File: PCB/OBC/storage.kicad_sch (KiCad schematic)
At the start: 2 parts, among them U1 W25Q128JVSIQ

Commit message: Watchdog
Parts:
- removed C3: C, symbol Device:C
- removed U1: W25Q128JVSIQ, SOIC_128JVSIQ_WIN, symbol W25Q128JVSIQ:W25Q128JVSIQ
- added C13: 100nF, symbol Device:C
- added U7: MAX6369KA+T, 21-0078H_MXM, symbol MAX6369KA+T:MAX6369KA+T
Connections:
- net +3V3: now also C13.1, U7.8 (VCC)
- net GND: now also C13.2, U7.2 (GND)
- new net SWD_NRST: U7.7 (*WDO)
- new net rst_wdi: U7.1 (WDI)
- new net set_0: U7.4 (SET0)
- new net set_1: U7.5 (SET1)
- new net set_2: U7.6 (SET2)

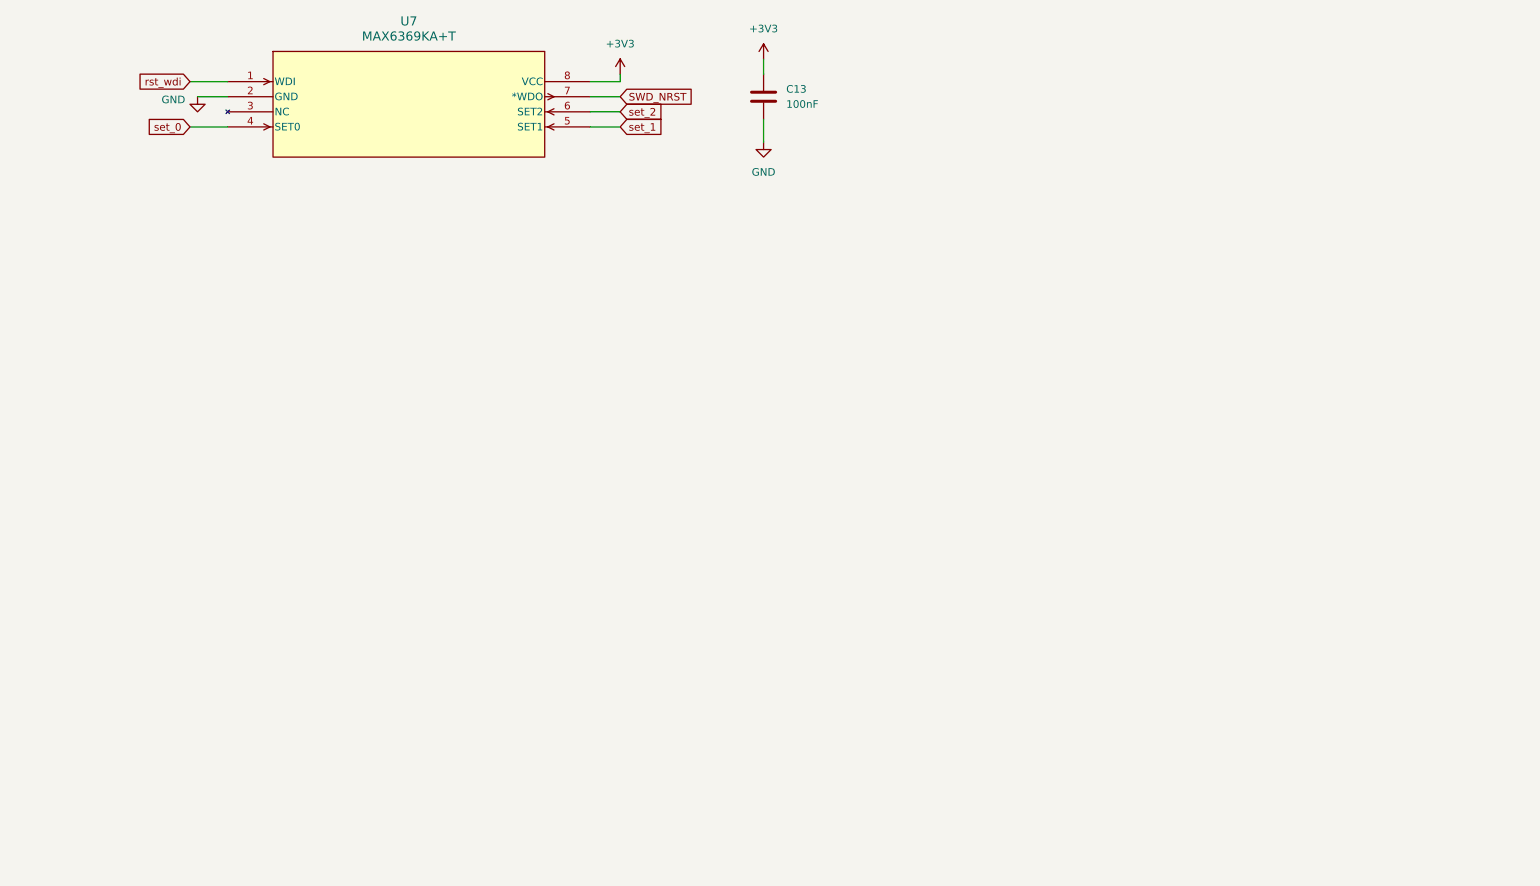
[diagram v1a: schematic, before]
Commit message: Colocacion de OCP, LDO
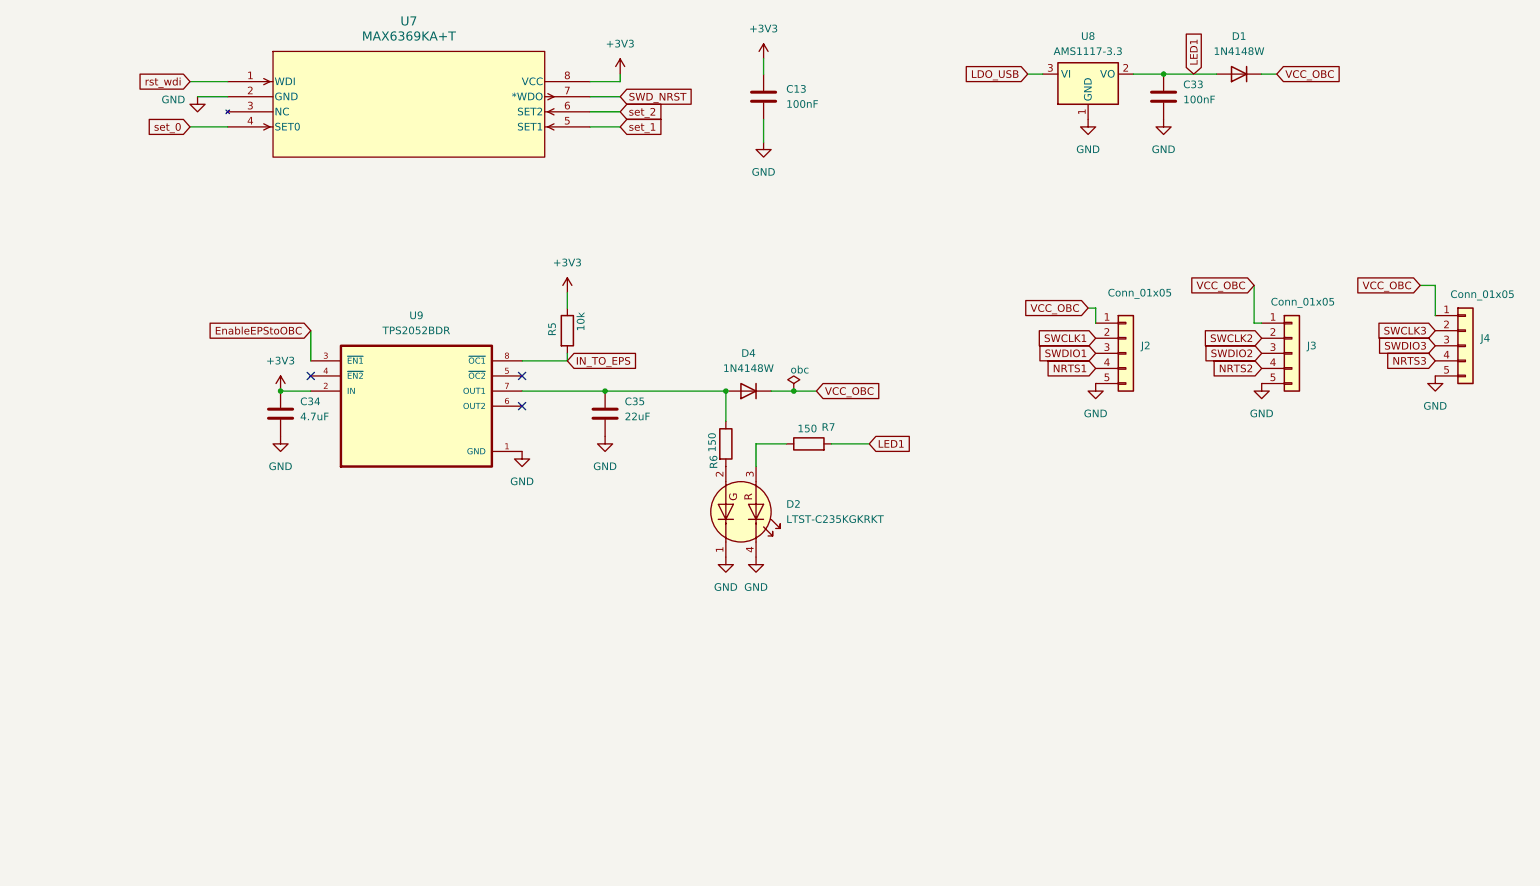
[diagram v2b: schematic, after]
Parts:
- added C33: 100nF, Capacitor_SMD:C_0805_2012Metric_Pad1.18x1.45mm_HandSolder, symbol Device:C
- added C34: 4.7uF, Capacitor_SMD:C_0805_2012Metric_Pad1.18x1.45mm_HandSolder, symbol Device:C
- added C35: 22uF, Capacitor_SMD:C_0805_2012Metric_Pad1.18x1.45mm_HandSolder, symbol Device:C
- added D1, D4: 1N4148W, Diode_SMD:D_SOD-123, symbol Diode:1N4148W
- added D2: LTST-C235KGKRKT, LED_SMD:LED_LiteOn_LTST-C235KGKRKT, symbol LED:LTST-C235KGKRKT
- added J2, J3, J4: Conn_01x05, Connector_PinHeader_2.54mm:PinHeader_1x05_P2.54mm_Vertical_SMD_Pin1Left, symbol Connector_Generic:Conn_01x05
- added R5: 10k, symbol Device:R
- added R6, R7: 150, symbol Device:R
- added U8: AMS1117-3.3, Package_TO_SOT_SMD:SOT-223-3_TabPin2, symbol Regulator_Linear:AMS1117-3.3
- added U9: TPS2052BDR, TPS2052BDR:SOIC127P599X175-8N, symbol TPS2052BDR:TPS2052BDR
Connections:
- net +3V3: now also C34.1, R5.1, U9.2 (IN)
- net GND: now also C33.2, C34.2, C35.2, D2.1 (K2), D2.4 (K1), J2.5 (Pin_5), J3.5 (Pin_5), J4.5 (Pin_5), U8.1 (GND), U9.1 (GND)
- new net: C35.1, D4.2 (A), R6.1, U9.7 (OUT1)
- new net: D2.3 (A1), R7.1
- new net: D2.2 (A2), R6.2
- new net EnableEPStoOBC: U9.3 (~{EN1})
- new net IN_TO_EPS: R5.2, U9.8 (~{OC1})
- new net LDO_USB: U8.3 (VI)
- new net LED1: C33.1, D1.2 (A), R7.2, U8.2 (VO)
- new net NRTS1: J2.4 (Pin_4)
- new net NRTS2: J3.4 (Pin_4)
- new net NRTS3: J4.4 (Pin_4)
- new net SWCLK1: J2.2 (Pin_2)
- new net SWCLK2: J3.2 (Pin_2)
- new net SWCLK3: J4.2 (Pin_2)
- new net SWDIO1: J2.3 (Pin_3)
- new net SWDIO2: J3.3 (Pin_3)
- new net SWDIO3: J4.3 (Pin_3)
- new net VCC_OBC: D1.1 (K), D4.1 (K), J2.1 (Pin_1), J3.1 (Pin_1), J4.1 (Pin_1)
- no-connect marks 0 -> 3

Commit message: Add: Can bus
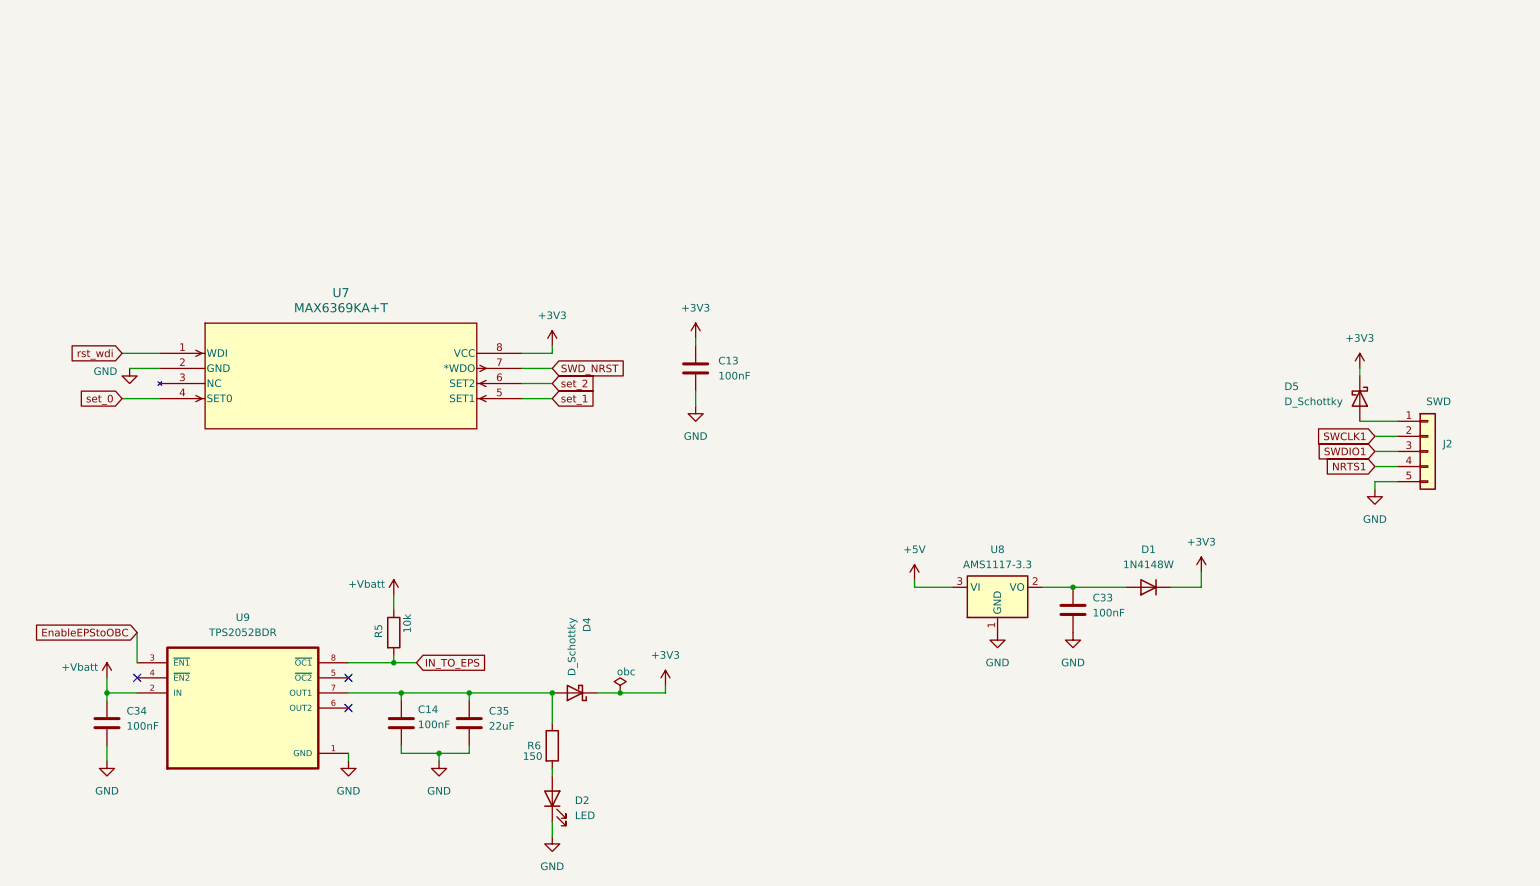
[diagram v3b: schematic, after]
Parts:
- removed D2: LTST-C235KGKRKT, LED_SMD:LED_LiteOn_LTST-C235KGKRKT, symbol LED:LTST-C235KGKRKT
- removed D4: 1N4148W, Diode_SMD:D_SOD-123, symbol Diode:1N4148W
- removed J3, J4: Conn_01x05, Connector_PinHeader_2.54mm:PinHeader_1x05_P2.54mm_Vertical_SMD_Pin1Left, symbol Connector_Generic:Conn_01x05
- removed R7: 150, symbol Device:R
- added C14: 100nF, Capacitor_SMD:C_0805_2012Metric_Pad1.18x1.45mm_HandSolder, symbol Device:C
- added D2: LED, symbol Device:LED
- added D4, D5: D_Schottky, symbol Device:D_Schottky
- C34: value 4.7uF -> 100nF
- J2: value Conn_01x05 -> SWD
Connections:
- net +3V3: now also D1.1 (K), D4.1 (K), D5.1 (K); no longer C34.1, R5.1, U9.2 (IN)
- net GND: now also C14.2, D2.1 (K)
- net at C35.1, R6.1, U9.7 (OUT1): now also C14.1, D4.2 (A)
- net at R6.2: now also D2.2 (A)
- net LDO_USB renamed +5V
- net LED1: no longer names the net of C33.1, D1.2 (A), U8.2 (VO)
- net VCC_OBC: no longer names the net of J2.1 (Pin_1)
- net VCC_OBC: now also D5.2 (A); no longer D1.1 (K)
- new net +Vbatt: C34.1, R5.1, U9.2 (IN)
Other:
- moved on the sheet: C13, C33, C34, C35, D1, J2, R5, R6, U7, U8, U9

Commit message: N
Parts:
- removed D1: 1N4148W, Diode_SMD:D_SOD-123, symbol Diode:1N4148W
- added D6: D_Schottky, symbol Device:D_Schottky
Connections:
- net +3V3: now also D6.1 (K)
- net at C33.1, U8.2 (VO): now also D6.2 (A)
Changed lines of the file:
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@@
+	)
+	(symbol
+		(lib_id "Device:D_Schottky")
+		(at 217.17 144.78 180)
+		(unit 1)
+		(exclude_from_sim no)
+		(in_bom yes)
+		(on_board yes)
+		(dnp no)
+		(property "Reference" "D6"
+			(at 219.202 132.08 90)
+			(effects
+				(font
+					(size 1.27 1.27)
+				)
+				(justify left)
+			)
+		)
+		(property "Value" "D_Schottky"
+			(at 216.662 132.08 90)
+			(effects
+				(font
+					(size 1.27 1.27)
+				)
+				(justify left)
+			)
+		)
+		(property "Footprint" ""
+			(at 217.17 144.78 0)
+			(effects
+				(font
+					(size 1.27 1.27)
+				)
+				(hide yes)
+			)
+		)
+		(property "Datasheet" "~"
+			(at 217.17 144.78 0)
+			(effects
+				(font
+					(size 1.27 1.27)
+				)
+				(hide yes)
+			)
+		)
+		(property "Description" "Schottky diode"
+			(at 217.17 144.78 0)
+			(effects
+				(font
+					(size 1.27 1.27)
+				)
+				(hide yes)
+			)
+		)
+		(pin "2"
+		)
+		(pin "1"
+		)
+		(instances
+			(project "OBC"
+				(path "/e2c03eef-3b12-44a7-ba52-633d5337a24a/50cd9bda-d2af-42b5-bb85-974edeb725b5"
+					(reference "D6")
+					(unit 1)
+				)
+			)
+		)
 	)
 	(symbol
@@
 					(unit 1)
 				)
-			)
-		)
-	)
-	(symbol
-		(lib_id "Diode:1N4148W")
-		(at 217.17 144.78 180)
-		(unit 1)
-		(exclude_from_sim no)
-		(in_bom yes)
-		(on_board yes)
-		(dnp no)
-		(fields_autoplaced yes)
-		(property "Reference" "D1"
-			(at 217.17 138.43 0)
-			(effects
-				(font
-					(size 1.27 1.27)
-				)
-			)
-		)
-		(property "Value" "1N4148W"
-			(at 217.17 140.97 0)
-			(effects
-				(font
-					(size 1.27 1.27)
-				)
-			)
-		)
-		(property "Footprint" "Diode_SMD:D_SOD-123"
-			(at 217.17 140.335 0)
-			(effects
-				(font
-					(size 1.27 1.27)
-				)
-				(hide yes)
-			)
-		)
-		(property "Datasheet" "https://www.vishay.com/docs/85748/1n4148w.pdf"
-			(at 217.17 144.78 0)
-			(effects
-				(font
-					(size 1.27 1.27)
-				)
-				(hide yes)
-			)
-		)
-		(property "Description" "75V 0.15A Fast Switching Diode, SOD-123"
-			(at 217.17 144.78 0)
-			(effects
-				(font
-					(size 1.27 1.27)
-				)
-				(hide yes)
-			)
-		)
-		(property "Sim.Device" "D"
-			(at 217.17 144.78 0)
-			(effects
-				(font
-					(size 1.27 1.27)
-				)
-				(hide yes)
-			)
-		)
-		(property "Sim.Pins" "1=K 2=A"
-			(at 217.17 144.78 0)
-			(effects
-				(font
-					(size 1.27 1.27)
-				)
-				(hide yes)
-			)
-		)
-		(pin "2"
-		)
-		(pin "1"
-		)
-		(instances
-			(project "OBC"
-				(path "/e2c03eef-3b12-44a7-ba52-633d5337a24a/50cd9bda-d2af-42b5-bb85-974edeb725b5"
-					(reference "D1")
-					(unit 1)
-				)
